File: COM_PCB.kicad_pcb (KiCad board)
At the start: 2 copper layers, 70 x 70 mm, 55 parts, among them J1 Conn_Coaxial, J2 SIM_Card, J3 ST_LINK, J4 Conn_Coaxial, J6 02x12, SW1 Reset, U1 STM32F401CEUx, U2 NEO-6M-0-001, U3 Ai-Thinker_Ra-02, Y1 MCSJK

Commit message: KiCad 0.3v
Improved aesthetics.
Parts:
- removed D2, D5, D6, D7: BLUE, LED_SMD:LED_0805_2012Metric_Pad1.15x1.40mm_HandSolder
- removed GND (x2), MISO, MOSI, RX (x3), SCK, SS, TX (x3): TestPoint, Connector_PinHeader_1.00mm:PinHeader_1x01_P1.00mm_Vertical
- removed GSM1: A6_GSM, A6:A6_GSM
- removed J4: Conn_Coaxial, Connector_Coaxial:SMA_Amphenol_132134-16_Vertical
- removed J6: 02x12, LOCAL:SAMTEC-SSW-112-02-X-D-RA
- removed R10, R8, R9: 75, Resistor_SMD:R_0805_2012Metric_Pad1.20x1.40mm_HandSolder
- removed R12: 12k, Resistor_SMD:R_0603_1608Metric
- removed R13: 12k, Resistor_SMD:R_0603_1608Metric_Pad0.98x0.95mm_HandSolder
- removed R6: 10k, Resistor_SMD:R_0603_1608Metric_Pad0.98x0.95mm_HandSolder
- removed SW1: Reset, button:little_button
- removed U1: STM32F401CEUx, Package_DFN_QFN:QFN-48-1EP_7x7mm_P0.5mm_EP5.6x5.6mm
- removed U3: Ai-Thinker_Ra-02, LOCAL:Ai-Thinker_Ra-02
- removed Y1: MCSJK, Crystal:Crystal_SMD_5032-4Pin_5.0x3.2mm
- added C17: 2.4pF, Capacitor_SMD:C_0402_1005Metric, F.Cu at (115.9, 77.9)
- added C18: 0.1uF, Capacitor_SMD:C_0603_1608Metric, F.Cu at (111.8, 90.7)
- added C19: 10uF, Capacitor_SMD:C_0603_1608Metric, F.Cu at (116.6, 87.6)
- added C20: 220uF, Capacitor_Tantalum_SMD:CP_EIA-3216-10_Kemet-I_Pad1.58x1.35mm_HandSolder, F.Cu at (149.0, 81.0)
- added C21: 0.1uF, Capacitor_SMD:C_0603_1608Metric, F.Cu at (147.9, 86.9)
- added C22: 220uF, Capacitor_Tantalum_SMD:CP_EIA-3216-10_Kemet-I_Pad1.58x1.35mm_HandSolder, F.Cu at (149.0, 84.1)
- added C23: 0.1uF, Capacitor_SMD:C_0603_1608Metric, F.Cu at (142.6, 90.0)
- added C24: 0.1uF, Capacitor_SMD:C_0603_1608Metric, F.Cu at (152.1, 65.5)
- added C25: 0.1uF, Capacitor_SMD:C_0603_1608Metric, F.Cu at (143.2, 69.9)
- added C26: 0.1uF, Capacitor_SMD:C_0603_1608Metric, F.Cu at (148.1, 65.5)
- added C27: 12.5pF, Capacitor_SMD:C_0603_1608Metric, F.Cu at (147.2, 68.0)
- added C28: 220nF, Capacitor_SMD:C_0603_1608Metric, F.Cu at (143.2, 67.4)
- added C29: 12.5pF, Capacitor_SMD:C_0603_1608Metric, F.Cu at (152.4, 63.0)
- added J8: ST_LINK, Connector_PinSocket_2.54mm:PinSocket_1x04_P2.54mm_Vertical, F.Cu at (138.9, 64.0)
- added L2: 33nH, Inductor_SMD:L_0402_1005Metric, F.Cu at (110.1, 77.9)
- added L3: 30nH, Inductor_SMD:L_0402_1005Metric, F.Cu at (110.1, 75.9)
- added L4: 36nH, Inductor_SMD:L_0402_1005Metric, F.Cu at (119.9, 67.7)
- added L5: 22nH, Inductor_SMD:L_0402_1005Metric, F.Cu at (123.9, 66.4)
- added L6: 62nH, Inductor_SMD:L_0402_1005Metric, F.Cu at (119.9, 69.7)
- added L7: 56nH, Inductor_SMD:L_0402_1005Metric, F.Cu at (113.0, 75.9)
- added L8: 27uH, Capacitor_SMD:C_0805_2012Metric_Pad1.18x1.45mm_HandSolder, F.Cu at (112.2, 84.8)
- added R3: 10, Capacitor_SMD:C_0603_1608Metric, F.Cu at (111.8, 93.2)
- added R7: 12k, Resistor_SMD:R_0603_1608Metric_Pad0.98x0.95mm_HandSolder, F.Cu at (148.2, 63.0)
- added U5: LM4040DBZ-3, Package_TO_SOT_SMD:SOT-23, F.Cu at (143.6, 63.9)
- added X1: TCXO 26 MHz, Crystal:Crystal_SMD_2016-4Pin_2.0x1.6mm, F.Cu at (124.4, 63.5)
- C1: value 0.1uF -> 4.7uF
- C10: value 0.1uF -> 100pF; footprint Capacitor_SMD:C_0603_1608Metric -> Capacitor_SMD:C_0402_1005Metric
- C11: value 220uF -> 10pF; footprint Capacitor_Tantalum_SMD:CP_EIA-3216-10_Kemet-I_Pad1.58x1.35mm_HandSolder -> Capacitor_SMD:C_0402_1005Metric
- C12: value 0.1uF -> 680pF; footprint Capacitor_SMD:C_0603_1608Metric -> Capacitor_SMD:C_0402_1005Metric
- C13: value 22pF -> 680pF; footprint Capacitor_SMD:C_0603_1608Metric -> Capacitor_SMD:C_0402_1005Metric
- C14: value 22pF -> 10pF; footprint Capacitor_SMD:C_0603_1608Metric -> Capacitor_SMD:C_0402_1005Metric
- C15: value 220nF -> 680pF; footprint Capacitor_SMD:C_0603_1608Metric -> Capacitor_SMD:C_0402_1005Metric
- C16: value 4.7uF -> 4.7pF; footprint Capacitor_SMD:C_0603_1608Metric -> Capacitor_SMD:C_0402_1005Metric
- C2: value 220uF -> 4.7uF; footprint Capacitor_Tantalum_SMD:CP_EIA-3216-10_Kemet-I_Pad1.58x1.35mm_HandSolder -> Capacitor_SMD:C_0603_1608Metric
- C3, C4, C5: footprint Capacitor_SMD:C_0603_1608Metric -> Capacitor_SMD:C_0402_1005Metric
- C6: value 0.1uF -> 9.1pF; footprint Capacitor_SMD:C_0603_1608Metric -> Capacitor_SMD:C_0402_1005Metric
- C7: value 0.1uF -> 15pF; footprint Capacitor_SMD:C_0603_1608Metric -> Capacitor_SMD:C_0402_1005Metric
- C8: value 10uF -> 10nF; footprint Capacitor_SMD:C_0603_1608Metric -> Capacitor_SMD:C_0402_1005Metric
- C9: value 10uF -> 12pF; footprint Capacitor_SMD:C_0603_1608Metric -> Capacitor_SMD:C_0402_1005Metric
- J1: value Conn_Coaxial -> SMA
- J2: value SIM_Card -> SMA; footprint footprints:MOLEX_78800-0001 -> Connector_Coaxial:SMA_Amphenol_132134-16_Vertical
- J3: value ST_LINK -> SMA; footprint Connector_PinSocket_2.54mm:PinSocket_1x04_P2.54mm_Vertical -> Connector_Coaxial:SMA_Amphenol_132134-16_Vertical
- L1: value 27uH -> 220nH; footprint Capacitor_SMD:C_0805_2012Metric_Pad1.18x1.45mm_HandSolder -> Inductor_SMD:L_0603_1608Metric
- R1: value 10k -> 24; footprint Capacitor_SMD:C_0603_1608Metric -> Resistor_SMD:R_0603_1608Metric
- R2: value 75 -> 1k; footprint Resistor_SMD:R_0805_2012Metric_Pad1.20x1.40mm_HandSolder -> Resistor_SMD:R_0603_1608Metric_Pad0.98x0.95mm_HandSolder
- R4: value 1k -> 10k; footprint Resistor_SMD:R_0603_1608Metric_Pad0.98x0.95mm_HandSolder -> Capacitor_SMD:C_0603_1608Metric
- R5: value 10 -> 12k; footprint Capacitor_SMD:C_0603_1608Metric -> Resistor_SMD:R_0603_1608Metric
- U2: value NEO-6M-0-001 -> AS179-92LF; footprint footprints:XCVR_NEO-6M-GPS -> Package_TO_SOT_SMD:SOT-363_SC-70-6
- moved J2 58.5 mm to (105.1, 88.0), turned to 0 degrees
- moved J1 52.8 mm to (106.7, 66.0), turned to 0 degrees
- moved R1 47.8 mm to (120.5, 63.0)
- moved C10 47.4 mm to (127.8, 62.7)
- moved C1 47.1 mm to (106.7, 76.2)
- moved J3 43.0 mm to (141.2, 84.1), turned to 0 degrees
- moved R4 39.7 mm to (138.6, 90.0), turned to 0 degrees
- moved C9 39.2 mm to (122.8, 68.3)
- moved R5 35.2 mm to (143.2, 72.4), turned to 0 degrees
- moved C2 35.2 mm to (106.7, 78.7), turned to 0 degrees
- moved C11 28.7 mm to (113.0, 77.9), turned to 0 degrees
- moved C6 28.5 mm to (118.8, 75.9), turned to 0 degrees
- moved C12 28.1 mm to (119.9, 73.7)
- moved C5 27.9 mm to (125.7, 70.3), turned to 0 degrees
- moved R2 27.8 mm to (116.8, 84.6), turned to 0 degrees
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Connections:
- C1 pad 1: (no net) -> +3V3
- C1 pad 2: (no net) -> GND
- C10 pad 1: (no net) -> Net-(C10-Pad1)
- C10 pad 2: (no net) -> /SI4463/XOUT
- C11 pad 1: (no net) -> GND
- C11 pad 2: (no net) -> Net-(C11-Pad2)
- C12 pad 1: (no net) -> Net-(C12-Pad1)
- C12 pad 2: (no net) -> /SI4463/TX
- C13 pad 1: (no net) -> /SI4463/RX
- C13 pad 2: (no net) -> Net-(C13-Pad2)
- C14 pad 1: (no net) -> /SI4463/TX
- C14 pad 2: (no net) -> /SI4463/TX_F
- C15 pad 1: (no net) -> Net-(C15-Pad1)
- C15 pad 2: (no net) -> /SI4463/ANT
- C16 pad 1: (no net) -> GND
- C16 pad 2: (no net) -> /SI4463/RXp
- C2 pad 1: (no net) -> +3V3
- C2 pad 2: (no net) -> GND
- C3 pad 1: (no net) -> +3V3
- C3 pad 2: (no net) -> GND
- C4 pad 1: (no net) -> +3V3
- C4 pad 2: (no net) -> GND
- C5 pad 1: (no net) -> GND
- C5 pad 2: (no net) -> +3V3
- C6 pad 1: (no net) -> Net-(C6-Pad1)
- C6 pad 2: (no net) -> /SI4463/TX_UM
- C7 pad 1: (no net) -> GND
- C7 pad 2: (no net) -> /SI4463/TX_M
- C8 pad 1: (no net) -> GND
- C8 pad 2: (no net) -> +3V3
- C9 pad 1: (no net) -> GND
- C9 pad 2: (no net) -> Net-(C9-Pad2)
- D1 pad 1: (no net) -> GND
- D1 pad 2: (no net) -> Net-(D1-Pad2)
- J1 pad 1: (no net) -> /SI4463/ANT
- J1 pad 2: (no net) -> GND
- J2 pad 1: (no net) -> /GPS/ANT
- J2 pad 2: (no net) -> GND
- J3 pad 1: (no net) -> /GPRS/ANT
- J3 pad 2: (no net) -> GND
- L1 pad 1: (no net) -> /SI4463/TX_UM
- L1 pad 2: (no net) -> Net-(L1-Pad2)
- R1 pad 1: (no net) -> +3V3
- R1 pad 2: (no net) -> Net-(L1-Pad2)
- R2 pad 1: (no net) -> Net-(R2-Pad1)
- R2 pad 2: (no net) -> Net-(D1-Pad2)
- R4 pad 1: (no net) -> +4V
- R4 pad 2: (no net) -> /GPRS/GSM_RST
- R5 pad 1: (no net) -> /MCU/SW_CLK
- R5 pad 2: (no net) -> GND
- U2 pad 1: (no net) -> Net-(C12-Pad1)
- U2 pad 2: (no net) -> GND
- U2 pad 3: (no net) -> Net-(C13-Pad2)
- U2 pad 4: (no net) -> /SI4463/GPIO2
- U2 pad 5: (no net) -> Net-(C15-Pad1)
- U2 pad 6: (no net) -> /SI4463/GPIO3
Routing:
- net (no net): track 1353.2 -> 0.00 mm, vias 154 -> 0
- removed copper zone on B.Cu, net (none)
- removed copper zone on F.Cu, net (none)
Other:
- board size 70 x 70 mm -> 63.5 x 40.6 mm
- board text removed: "CARD"
- board text removed: "COM"
- board text removed: "GND"
- board text removed: "GPS-6M-NEO"
- board text removed: "IRBE-5"
- board text removed: "LORA_MODULE"
- board text removed: "Physical connector"
- board text removed: "RST"
- board text removed: "SIM"
- board text removed: "SW_CLK"
- board text removed: "SW_IO"

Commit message: 0.1v COM_PCB KiCad
First iteration of COM PCB.
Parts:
- removed C25, C26: 0.1uF, Capacitor_SMD:C_0603_1608Metric
- removed C28: 220nF, Capacitor_SMD:C_0603_1608Metric
- removed U5: LM4040DBZ-3, Package_TO_SOT_SMD:SOT-23
- added C30: 4.7uF, Capacitor_SMD:C_0603_1608Metric, F.Cu at (136.1, 111.8)
- added D3: LED, LED_SMD:LED_0603_1608Metric, F.Cu at (158.6, 74.4)
- added D4: LED, LED_SMD:LED_0603_1608Metric, F.Cu at (94.4, 74.4)
- added D5: LED, LED_SMD:LED_0603_1608Metric, F.Cu at (158.6, 72.8)
- added D6: LED, LED_SMD:LED_0603_1608Metric, F.Cu at (94.4, 72.8)
- added GSM1: A6_GSM, footprints:A6_GSM, F.Cu at (103.0, 107.9)
- added H1: Spacer, MountingHole:MountingHole_3.2mm_M3, F.Cu at (96.4, 68.2)
- added H2: Spacer, MountingHole:MountingHole_3.2mm_M3, F.Cu at (156.4, 68.2)
- added J4: Card_Holder, footprints:MOLEX_78800-0001, F.Cu at (101.9, 85.4)
- added J5: BackBone, Connector_PinSocket_2.54mm:PinSocket_2x10_P2.54mm_Horizontal, F.Cu at (115.0, 120.5)
- added J6: D1, Connector_PinSocket_2.54mm:PinSocket_1x08_P2.54mm_Horizontal, F.Cu at (122.3, 73.7)
- added J7: D2, Connector_PinSocket_2.54mm:PinSocket_1x08_P2.54mm_Horizontal, F.Cu at (148.3, 73.7)
- added R11: 120, Resistor_SMD:R_0603_1608Metric, F.Cu at (153.0, 74.4)
- added R12: 120, Resistor_SMD:R_0603_1608Metric, F.Cu at (100.0, 74.4)
- added R13: 120, Resistor_SMD:R_0603_1608Metric, F.Cu at (153.0, 72.8)
- added R14: 120, Resistor_SMD:R_0603_1608Metric, F.Cu at (100.0, 72.8)
- added U1: SI4463, Package_DFN_QFN:QFN-20-1EP_4x4mm_P0.5mm_EP2.6x2.6mm_ThermalVias, F.Cu at (126.2, 90.6)
- added U3: NEO-6M-0-001, footprints:XCVR_NEO-6M-GPS, F.Cu at (147.8, 110.6)
- added U4: STM32G071GBU, Package_DFN_QFN:QFN-28_4x4mm_P0.5mm, F.Cu at (121.6, 109.2)
- added Y1: FC-135R_32.7680KA-AG0, footprints:XTAL_FC-135R_32.7680KA-AG0, F.Cu at (117.0, 114.1)
- C19: value 10uF -> 4.7uF
- C20, C22: footprint Capacitor_Tantalum_SMD:CP_EIA-3216-10_Kemet-I_Pad1.58x1.35mm_HandSolder -> Capacitor_Tantalum_SMD:CP_EIA-3528-21_Kemet-B
- C8: value 10nF -> 100nF
- J1, J2, J3: moved to B.Cu
- J8: value ST_LINK -> BMI-S-205-C; footprint Connector_PinSocket_2.54mm:PinSocket_1x04_P2.54mm_Vertical -> RF_Shielding:Laird_Technologies_BMI-S-205-F_38.10x25.40mm
- L8: value 27uH -> 30uH
- R2: value 1k -> 12k
- R4: value 10k -> 12k
- X1: value TCXO 26 MHz -> TCXO 30 MHz
- moved J2 61.8 mm to (153.7, 126.2), turned to 90 degrees
- moved C29 61.4 mm to (115.2, 111.9), turned to 45 degrees
- moved J3 60.0 mm to (98.9, 126.6), turned to 180 degrees
- moved R7 58.5 mm to (124.1, 116.2), turned to 90 degrees
- moved C24 57.7 mm to (122.2, 114.8), turned to 90 degrees
- moved C22 57.3 mm to (110.2, 126.3)
- moved C20 57.1 mm to (110.2, 122.9)
- moved C27 55.4 mm to (119.2, 115.8), turned to -135 degrees
- moved J1 54.0 mm to (155.0, 90.1), turned to 180 degrees
- moved L8 53.8 mm to (152.7, 120.4), turned to 180 degrees
- moved D1 48.7 mm to (143.1, 125.6), turned to 90 degrees
- moved U2 46.7 mm to (147.4, 90.1)
- moved R3 46.5 mm to (149.9, 119.9), turned to -90 degrees
- moved R2 45.2 mm to (143.0, 121.4), turned to -90 degrees
- moved C23 43.7 mm to (111.2, 120.5)
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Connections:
- R5 pad 1: /MCU/SW_CLK -> /IO/SW_CLK
- R7 pad 2: /MCU/~{RST} -> /IO/~{RST}
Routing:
- net +3V3: track 0.00 -> 132.5 mm, vias 0 -> 6
- net /GPS/GPS_TX: track 0.00 -> 93.3 mm, vias 0 -> 3
- net /GPS/GPS_RX: track 0.00 -> 88.8 mm, vias 0 -> 5
- net /MCU/LED1: track 0.00 -> 82.7 mm, vias 0 -> 6
- net /GPRS/GSM_RX: track 0.00 -> 77.2 mm, vias 0 -> 3
- net /GPRS/GSM_TX: track 0.00 -> 76.8 mm, vias 0 -> 3
- net /MCU/LED3: track 0.00 -> 74.6 mm, vias 0 -> 4
- net +4V: track 0.00 -> 72.1 mm, vias 0 -> 3
- net /IO/RF_NSS: track 0.00 -> 70.2 mm, vias 0 -> 2
- net /IO/RF_MOSI: track 0.00 -> 67.1 mm, vias 0 -> 2
- net /IO/RF_MISO: track 0.00 -> 63.4 mm, vias 0 -> 2
- net /IO/RF_SCK: track 0.00 -> 62.0 mm, vias 0 -> 1
- net /IO/~{RST}: track 0.00 -> 46.5 mm, vias 0 -> 2
- net /MCU/LED2: track 0.00 -> 45.4 mm, vias 0 -> 2
- net /MCU/LED0: track 0.00 -> 44.2 mm, vias 0 -> 2
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- added copper zone on F.Cu, net (none)
- added copper zone on F.Cu, net +3V3
- added copper zone on F.Cu, net +4V
- added copper zone on B.Cu, net GND
- added copper zone on F.Cu, net GND
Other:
- board size 63.5 x 40.6 mm -> 70 x 70 mm
- board text added: "Physical connector"

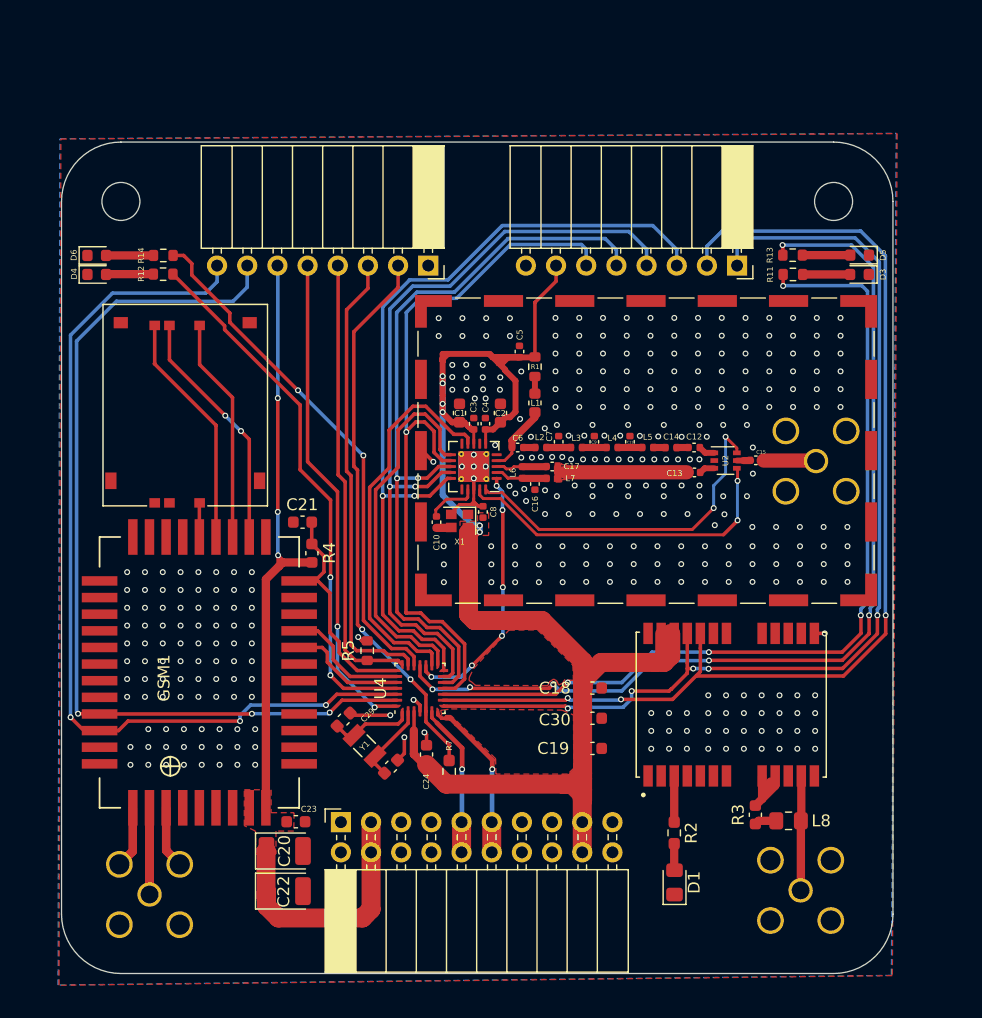
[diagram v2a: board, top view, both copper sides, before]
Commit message: solved issues
Crystal changes and some routing.
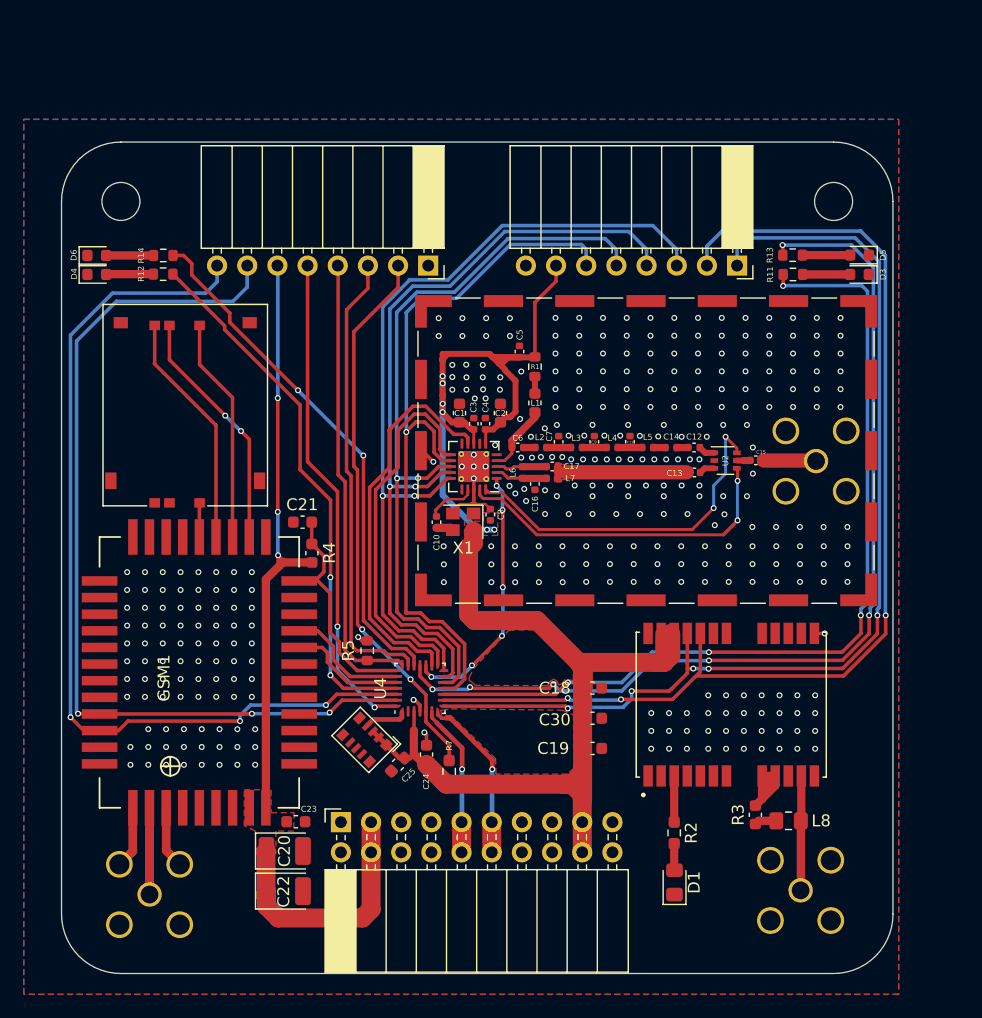
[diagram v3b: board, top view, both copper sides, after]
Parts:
- removed C27, C29: 12.5pF, Capacitor_SMD:C_0603_1608Metric
- added C25: 0.1uF, Capacitor_SMD:C_0603_1608Metric, F.Cu at (119.8, 115.7)
- X1: footprint Crystal:Crystal_SMD_2016-4Pin_2.0x1.6mm -> Crystal:Crystal_SMD_2520-4Pin_2.5x2.0mm
- Y1: value FC-135R_32.7680KA-AG0 -> TG-3541CE; footprint footprints:XTAL_FC-135R_32.7680KA-AG0 -> footprints:Oscillator_SMD_SeikoEpson_TG-3541CE_3.2x2.5mm
- moved C8 0.66 mm to (127.5, 94.6)
- moved Y1 0.51 mm to (117.0, 113.6)
- moved X1 0.31 mm to (125.3, 95.2)
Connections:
- U4 pad 2: /MCU/OSC32_IN -> unconnected-(U4-Pad2)
- Y1 pad 1: /MCU/OSC32_IN -> +3V3
- Y1 pad 2: /MCU/OSC32_OUT -> +3V3
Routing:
- net /MCU/OSC32_IN: track 6.68 -> 0.00 mm
- net +3V3: track 132.5 -> 138.3 mm
- net GND: track 38.4 -> 34.4 mm, vias 359 -> 357
- net /MCU/OSC32_OUT: track 7.00 -> 3.67 mm
- net Net-(R3-Pad1): track 6.23 -> 7.45 mm

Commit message: V1
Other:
- board text added: "MADE BY BASEMENT PROJECT WASSUP COM BOARD V1"
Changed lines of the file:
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@@
   )
   (paper "A4")
+  (title_block
+    (title "COM_BOARD")
+    (date "%%date%%")
+    (rev "%%version%%")
+  )
   (layers
     (0 "F.Cu" signal)
@@
       (outputformat 1)
       (mirror false)
-      (drillshape 1)
+      (drillshape 0)
       (scaleselection 1)
-      (outputdirectory "")
+      (outputdirectory "gerber/")
     )
   )
@@
     (fp_line (start -1 -0.3) (end -1 0.6) (layer "F.Fab") (width 0.1))
     (fp_line (start 1 -0.6) (end -0.7 -0.6) (layer "F.Fab") (width 0.1))
-    (pad "1" smd roundrect (at -1.025 0 90) (size 1.15 1.4) (layers "F.Cu" "F.Paste" "F.Mask") (roundrect_rratio 0.217391)
+    (pad "1" smd roundrect (at -1.025 0 90) (size 1.15 1.4) (layers "F.Cu" "F.Paste" "F.Mask") (roundrect_rratio 0.2173913043)
       (net 2 "GND") (pinfunction "K") (pintype "passive"))
-    (pad "2" smd roundrect (at 1.025 0 90) (size 1.15 1.4) (layers "F.Cu" "F.Paste" "F.Mask") (roundrect_rratio 0.217391)
+    (pad "2" smd roundrect (at 1.025 0 90) (size 1.15 1.4) (layers "F.Cu" "F.Paste" "F.Mask") (roundrect_rratio 0.2173913043)
       (net 24 "Net-(D1-Pad2)") (pinfunction "A") (pintype "passive"))
     (model "${KICAD6_3DMODEL_DIR}/LED_SMD.3dshapes/LED_0805_2012Metric.wrl"
@@
     (fp_line (start 1 -0.625) (end 1 0.625) (layer "F.Fab") (width 0.1))
     (fp_line (start 1 0.625) (end -1 0.625) (layer "F.Fab") (width 0.1))
-    (pad "1" smd roundrect (at -1.0375 0 180) (size 1.175 1.45) (layers "F.Cu" "F.Paste" "F.Mask") (roundrect_rratio 0.212766)
+    (pad "1" smd roundrect (at -1.0375 0 180) (size 1.175 1.45) (layers "F.Cu" "F.Paste" "F.Mask") (roundrect_rratio 0.2127659574)
       (net 33 "/GPS/ANT") (pintype "passive"))
-    (pad "2" smd roundrect (at 1.0375 0 180) (size 1.175 1.45) (layers "F.Cu" "F.Paste" "F.Mask") (roundrect_rratio 0.212766)
+    (pad "2" smd roundrect (at 1.0375 0 180) (size 1.175 1.45) (layers "F.Cu" "F.Paste" "F.Mask") (roundrect_rratio 0.2127659574)
       (net 55 "Net-(L8-Pad2)") (pintype "passive"))
     (model "${KICAD6_3DMODEL_DIR}/Capacitor_SMD.3dshapes/C_0805_2012Metric.wrl"
@@
     (fp_line (start -1.75 1.4) (end 1.75 1.4) (layer "F.Fab") (width 0.1))
     (fp_line (start -1.05 -1.4) (end -1.75 -0.7) (layer "F.Fab") (width 0.1))
-    (pad "1" smd roundrect (at -1.5375 0) (size 1.325 2.35) (layers "F.Cu" "F.Paste" "F.Mask") (roundrect_rratio 0.188679)
+    (pad "1" smd roundrect (at -1.5375 0) (size 1.325 2.35) (layers "F.Cu" "F.Paste" "F.Mask") (roundrect_rratio 0.1886792453)
       (net 3 "+4V") (pintype "passive"))
-    (pad "2" smd roundrect (at 1.5375 0) (size 1.325 2.35) (layers "F.Cu" "F.Paste" "F.Mask") (roundrect_rratio 0.188679)
+    (pad "2" smd roundrect (at 1.5375 0) (size 1.325 2.35) (layers "F.Cu" "F.Paste" "F.Mask") (roundrect_rratio 0.1886792453)
       (net 2 "GND") (pintype "passive"))
     (model "${KICAD6_3DMODEL_DIR}/Capacitor_Tantalum_SMD.3dshapes/CP_EIA-3528-21_Kemet-B.wrl"
@@
     (fp_line (start -1 -2) (end 2 -2) (layer "F.Fab") (width 0.1))
     (fp_line (start -2 2) (end -2 -1) (layer "F.Fab") (width 0.1))
-    (pad "" smd roundrect (at 0.65 0.65 180) (size 1.13 1.13) (layers "F.Paste") (roundrect_rratio 0.221239))
-    (pad "" smd roundrect (at -0.65 -0.65 180) (size 1.13 1.13) (layers "F.Paste") (roundrect_rratio 0.221239))
-    (pad "" smd roundrect (at -0.65 0.65 180) (size 1.13 1.13) (layers "F.Paste") (roundrect_rratio 0.221239))
-    (pad "" smd roundrect (at 0.65 -0.65 180) (size 1.13 1.13) (layers "F.Paste") (roundrect_rratio 0.221239))
+    (pad "" smd roundrect (at 0.65 0.65 180) (size 1.13 1.13) (layers "F.Paste") (roundrect_rratio 0.2212389381))
+    (pad "" smd roundrect (at -0.65 -0.65 180) (size 1.13 1.13) (layers "F.Paste") (roundrect_rratio 0.2212389381))
+    (pad "" smd roundrect (at -0.65 0.65 180) (size 1.13 1.13) (layers "F.Paste") (roundrect_rratio 0.2212389381))
+    (pad "" smd roundrect (at 0.65 -0.65 180) (size 1.13 1.13) (layers "F.Paste") (roundrect_rratio 0.2212389381))
     (pad "1" smd roundrect (at -1.925 -1 180) (size 0.85 0.25) (layers "F.Cu" "F.Paste" "F.Mask") (roundrect_rratio 0.25)
       (net 61 "/MCU/RF_RST") (pinfunction "SDN") (pintype "input"))
@@
     (fp_line (start 1.75 -1.4) (end -1.05 -1.4) (layer "F.Fab") (width 0.1))
     (fp_line (start -1.75 1.4) (end 1.75 1.4) (layer "F.Fab") (width 0.1))
-    (pad "1" smd roundrect (at -1.5375 0) (size 1.325 2.35) (layers "F.Cu" "F.Paste" "F.Mask") (roundrect_rratio 0.188679)
+    (pad "1" smd roundrect (at -1.5375 0) (size 1.325 2.35) (layers "F.Cu" "F.Paste" "F.Mask") (roundrect_rratio 0.1886792453)
       (net 3 "+4V") (pintype "passive"))
-    (pad "2" smd roundrect (at 1.5375 0) (size 1.325 2.35) (layers "F.Cu" "F.Paste" "F.Mask") (roundrect_rratio 0.188679)
+    (pad "2" smd roundrect (at 1.5375 0) (size 1.325 2.35) (layers "F.Cu" "F.Paste" "F.Mask") (roundrect_rratio 0.1886792453)
       (net 2 "GND") (pintype "passive"))
     (model "${KICAD6_3DMODEL_DIR}/Capacitor_Tantalum_SMD.3dshapes/CP_EIA-3528-21_Kemet-B.wrl"
@@
   (gr_line (start 96.445 63.25) (end 156.445 63.25) (layer "Edge.Cuts") (width 0.05))
   (gr_line (start 156.445 133.25) (end 96.445 133.25) (layer "Edge.Cuts") (width 0.05))
+  (gr_text "MADE BY BASEMENT\nPROJECT WASSUP\nCOM BOARD\nV1\n" (at 126.665 98.471) (layer "B.SilkS")
+    (effects (font (size 3 3) (thickness 0.45)) (justify mirror))
+  )
   (gr_text "Physical connector" (at 126.4158 129.1336) (layer "Dwgs.User")
     (effects (font (size 1 1) (thickness 0.15)))
@@
     (connect_pads yes (clearance 0))
     (min_thickness 0.2)
-    (keepout (tracks allowed) (vias allowed) (pads allowed ) (copperpour not_allowed) (footprints allowed))
+    (keepout (tracks allowed) (vias allowed) (pads allowed) (copperpour not_allowed) (footprints allowed))
     (fill (thermal_gap 0.508) (thermal_bridge_width 0.508))
     (polygon
